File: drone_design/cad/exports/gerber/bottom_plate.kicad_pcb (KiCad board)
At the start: 2 copper layers, 120 x 120 mm, 4 parts

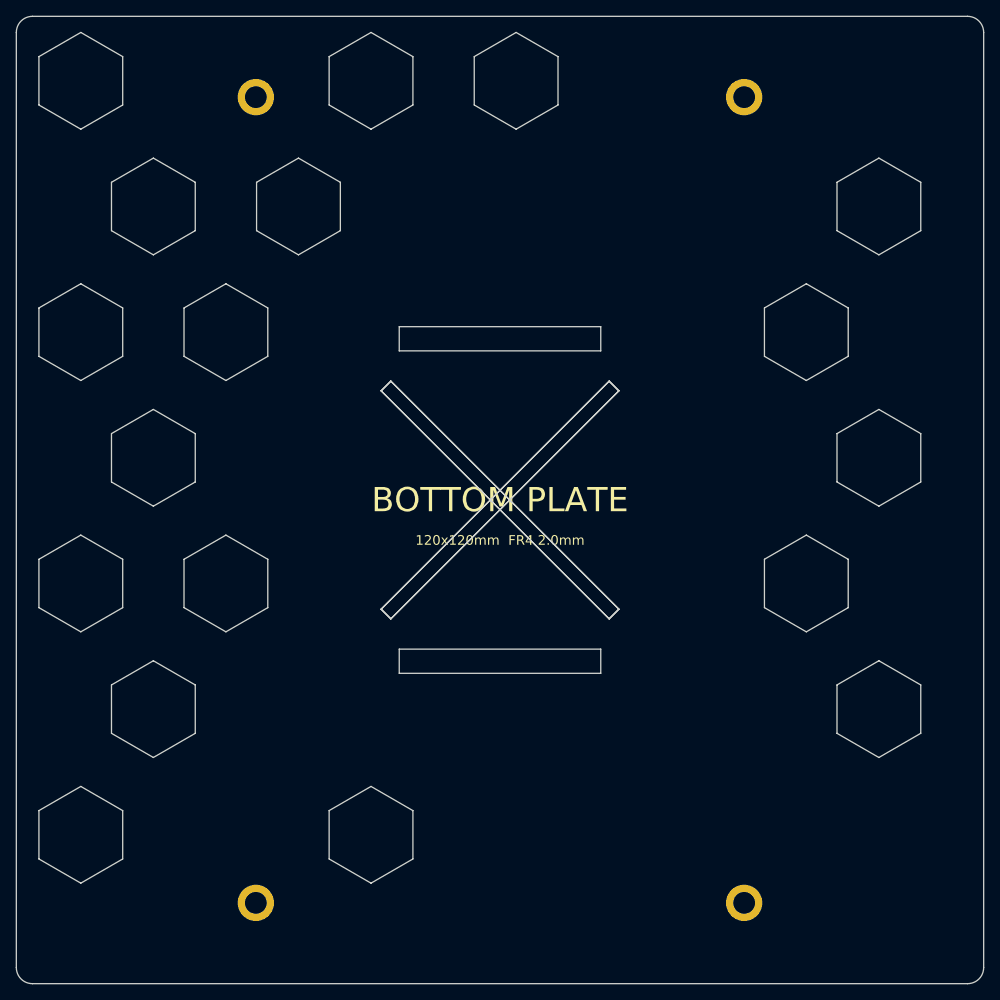
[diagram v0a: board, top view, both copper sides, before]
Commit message: feat: fix ToF bracket alignment, add motor mount to arm tips
- Fix all 6 ToF sensor/bracket positions with correct rotations
  so sensors sit flush against bracket tab faces, sensing outward
- Add circular motor mounting plate at arm tips (25mm dia)
  with 4x M2 bolt holes on 16mm circle + center shaft clearance
- Add matching M2 threaded holes to motor base plate model
- Rebuild all STLs and viewer (68 parts, 15.8 MB total)
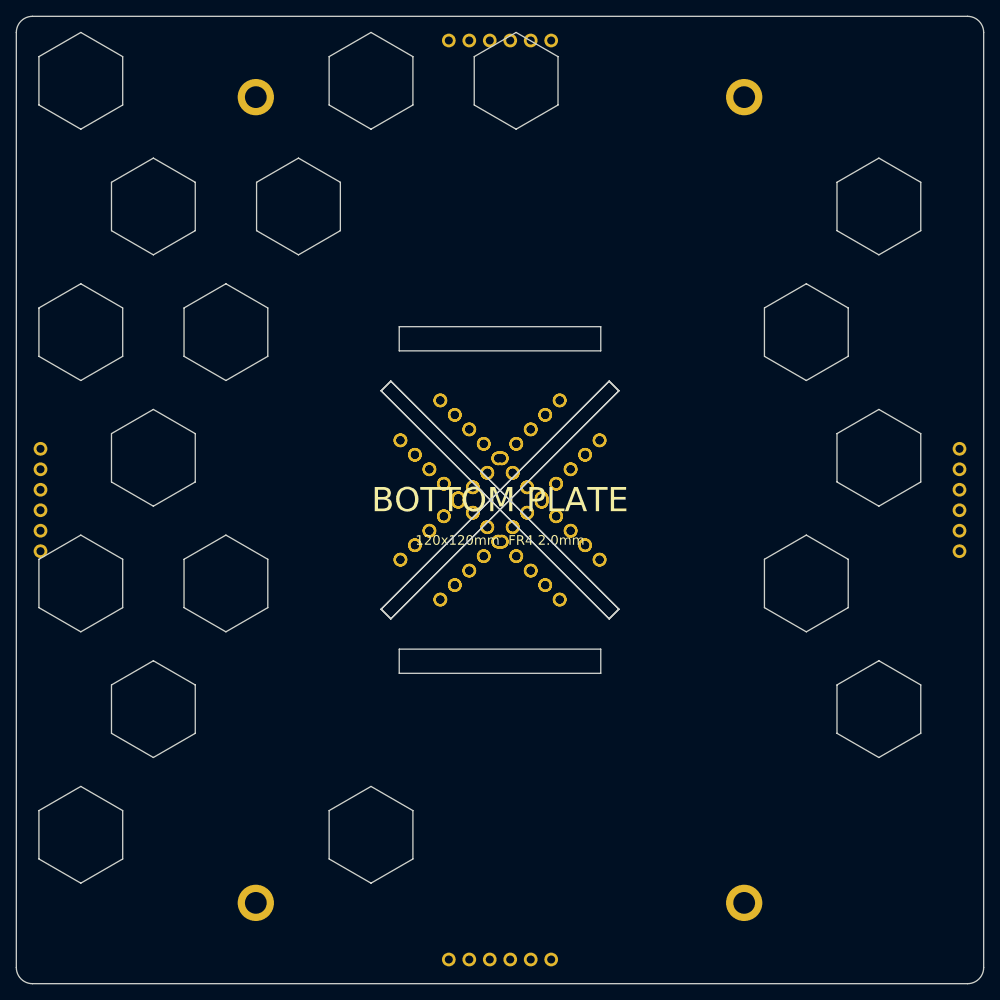
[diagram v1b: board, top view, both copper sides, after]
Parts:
- added ? (x2): , MountingHole:MountingHole_1.0mm, F.Cu at (1.58, -3.37)
- added ? (x2): , MountingHole:MountingHole_1.0mm, F.Cu at (12.4, -7.40)
- added ?: , MountingHole:MountingHole_1.0mm, F.Cu at (57.0, -6.35)
- added ?: , MountingHole:MountingHole_1.0mm, F.Cu at (57.0, -3.81)
- added ?: , MountingHole:MountingHole_1.0mm, F.Cu at (57.0, -1.27)
- added ?: , MountingHole:MountingHole_1.0mm, F.Cu at (57.0, 1.27)
- added ?: , MountingHole:MountingHole_1.0mm, F.Cu at (57.0, 3.81)
- added ?: , MountingHole:MountingHole_1.0mm, F.Cu at (57.0, 6.35)
- added ?: , MountingHole:MountingHole_1.0mm, F.Cu at (6.35, 57.0)
- added ?: , MountingHole:MountingHole_1.0mm, F.Cu at (3.81, 57.0)
- added ?: , MountingHole:MountingHole_1.0mm, F.Cu at (1.27, 57.0)
- added ? (x2): , MountingHole:MountingHole_1.0mm, F.Cu at (3.37, -1.58)
- added ?: , MountingHole:MountingHole_1.0mm, F.Cu at (-1.27, 57.0)
- added ?: , MountingHole:MountingHole_1.0mm, F.Cu at (-3.81, 57.0)
- added ?: , MountingHole:MountingHole_1.0mm, F.Cu at (-6.35, 57.0)
- added ?: , MountingHole:MountingHole_1.0mm, F.Cu at (-57.0, 6.35)
- added ?: , MountingHole:MountingHole_1.0mm, F.Cu at (-57.0, 3.81)
- added ?: , MountingHole:MountingHole_1.0mm, F.Cu at (-57.0, 1.27)
- added ?: , MountingHole:MountingHole_1.0mm, F.Cu at (-57.0, -1.27)
- added ?: , MountingHole:MountingHole_1.0mm, F.Cu at (-57.0, -3.81)
- added ?: , MountingHole:MountingHole_1.0mm, F.Cu at (-57.0, -6.35)
- added ?: , MountingHole:MountingHole_1.0mm, F.Cu at (-6.35, -57.0)
- added ? (x2): , MountingHole:MountingHole_1.0mm, F.Cu at (5.17, 0.22)
- added ?: , MountingHole:MountingHole_1.0mm, F.Cu at (-3.81, -57.0)
- added ?: , MountingHole:MountingHole_1.0mm, F.Cu at (-1.27, -57.0)
- added ?: , MountingHole:MountingHole_1.0mm, F.Cu at (1.27, -57.0)
- added ?: , MountingHole:MountingHole_1.0mm, F.Cu at (3.81, -57.0)
- added ?: , MountingHole:MountingHole_1.0mm, F.Cu at (6.35, -57.0)
- added ? (x2): , MountingHole:MountingHole_1.0mm, F.Cu at (6.96, 2.02)
- added ? (x2): , MountingHole:MountingHole_1.0mm, F.Cu at (8.76, 3.81)
- added ? (x2): , MountingHole:MountingHole_1.0mm, F.Cu at (10.6, 5.61)
- added ? (x2): , MountingHole:MountingHole_1.0mm, F.Cu at (12.4, 7.40)
- added ? (x2): , MountingHole:MountingHole_1.0mm, F.Cu at (-12.4, -7.40)
- added ? (x2): , MountingHole:MountingHole_1.0mm, F.Cu at (-10.6, -5.61)
- added ? (x2): , MountingHole:MountingHole_1.0mm, F.Cu at (-8.76, -3.81)
- added ? (x2): , MountingHole:MountingHole_1.0mm, F.Cu at (-6.96, -2.02)
- added ? (x2): , MountingHole:MountingHole_1.0mm, F.Cu at (-5.17, -0.22)
- added ? (x2): , MountingHole:MountingHole_1.0mm, F.Cu at (-3.37, 1.58)
- added ? (x2): , MountingHole:MountingHole_1.0mm, F.Cu at (-1.58, 3.37)
- added ? (x2): , MountingHole:MountingHole_1.0mm, F.Cu at (0.22, 5.17)
- added ? (x2): , MountingHole:MountingHole_1.0mm, F.Cu at (2.02, 6.96)
- added ? (x2): , MountingHole:MountingHole_1.0mm, F.Cu at (3.81, 8.76)
- added ? (x2): , MountingHole:MountingHole_1.0mm, F.Cu at (5.61, 10.6)
- added ? (x2): , MountingHole:MountingHole_1.0mm, F.Cu at (7.40, 12.4)
- added ? (x2): , MountingHole:MountingHole_1.0mm, F.Cu at (10.6, -5.61)
- added ? (x2): , MountingHole:MountingHole_1.0mm, F.Cu at (8.76, -3.81)
- added ? (x2): , MountingHole:MountingHole_1.0mm, F.Cu at (6.96, -2.02)
- added ? (x2): , MountingHole:MountingHole_1.0mm, F.Cu at (5.17, -0.22)
- added ? (x2): , MountingHole:MountingHole_1.0mm, F.Cu at (3.37, 1.58)
- added ? (x2): , MountingHole:MountingHole_1.0mm, F.Cu at (1.58, 3.37)
- added ? (x2): , MountingHole:MountingHole_1.0mm, F.Cu at (-0.22, 5.17)
- added ? (x2): , MountingHole:MountingHole_1.0mm, F.Cu at (-2.02, 6.96)
- added ? (x2): , MountingHole:MountingHole_1.0mm, F.Cu at (-3.81, 8.76)
- added ? (x2): , MountingHole:MountingHole_1.0mm, F.Cu at (-5.61, 10.6)
- added ? (x2): , MountingHole:MountingHole_1.0mm, F.Cu at (-7.40, 12.4)
- added ? (x2): , MountingHole:MountingHole_1.0mm, F.Cu at (7.40, -12.4)
- added ? (x2): , MountingHole:MountingHole_1.0mm, F.Cu at (5.61, -10.6)
- added ? (x2): , MountingHole:MountingHole_1.0mm, F.Cu at (3.81, -8.76)
- added ? (x2): , MountingHole:MountingHole_1.0mm, F.Cu at (2.02, -6.96)
- added ? (x2): , MountingHole:MountingHole_1.0mm, F.Cu at (0.22, -5.17)
- added ? (x2): , MountingHole:MountingHole_1.0mm, F.Cu at (-1.58, -3.37)
- added ? (x2): , MountingHole:MountingHole_1.0mm, F.Cu at (-3.37, -1.58)
- added ? (x2): , MountingHole:MountingHole_1.0mm, F.Cu at (-5.17, 0.22)
- added ? (x2): , MountingHole:MountingHole_1.0mm, F.Cu at (-6.96, 2.02)
- added ? (x2): , MountingHole:MountingHole_1.0mm, F.Cu at (-7.40, -12.4)
- added ? (x2): , MountingHole:MountingHole_1.0mm, F.Cu at (-8.76, 3.81)
- added ? (x2): , MountingHole:MountingHole_1.0mm, F.Cu at (-10.6, 5.61)
- added ? (x2): , MountingHole:MountingHole_1.0mm, F.Cu at (-12.4, 7.40)
- added ? (x2): , MountingHole:MountingHole_1.0mm, F.Cu at (-5.61, -10.6)
- added ? (x2): , MountingHole:MountingHole_1.0mm, F.Cu at (-3.81, -8.76)
- added ? (x2): , MountingHole:MountingHole_1.0mm, F.Cu at (-0.22, -5.17)
- added ? (x2): , MountingHole:MountingHole_1.0mm, F.Cu at (-2.02, -6.96)
